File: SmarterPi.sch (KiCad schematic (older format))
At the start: 2 parts, among them J1 Raspberry_Pi_2_3, J2 RJ10

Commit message: Reed
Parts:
- added J3, J4: Screw_Terminal_01x02, TerminalBlock:TerminalBlock_bornier-2_P5.08mm, symbol Connector:Screw_Terminal_01x02
- added R1: 2k4, Resistor_THT:R_Axial_DIN0207_L6.3mm_D2.5mm_P10.16mm_Horizontal, symbol Device:R
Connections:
- net +3V3: now also J3.1 (Pin_1); no longer J1.17 (3V3)
- net GND: now also R1.1
- net REED: now reaches J1.15 (GPIO22)
- net REED: now also J3.2 (Pin_2), R1.2
- no-connect marks 0 -> 3
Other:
- note added: "RJ10 connector for smart meter"
- note added: "Reed connector for gas meter"
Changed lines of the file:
@@
 L power:+3.3V #PWR05
 U 1 1 6019C9EE
-P 5900 2250
-F 0 "#PWR05" H 5900 2100 50  0001 C CNN
-F 1 "+3.3V" H 5915 2423 50  0000 C CNN
-F 2 "" H 5900 2250 50  0001 C CNN
-F 3 "" H 5900 2250 50  0001 C CNN
-	1    5900 2250
+P 5800 2250
+F 0 "#PWR05" H 5800 2100 50  0001 C CNN
+F 1 "+3.3V" H 5815 2423 50  0000 C CNN
+F 2 "" H 5800 2250 50  0001 C CNN
+F 3 "" H 5800 2250 50  0001 C CNN
+	1    5800 2250
 	1    0    0    -1
 $EndComp
 Wire Wire Line
-	5900 2250 5900 2450
-Wire Wire Line
 	5800 2450 5800 2250
-Wire Wire Line
-	5800 2250 5900 2250
-Connection ~ 5900 2250
 $Comp
 L power:PWR_FLAG #FLG01
@@
 Wire Wire Line
 	3350 3000 2950 3000
-Text GLabel 3350 2900 2    50   Input ~ 0
+Wire Wire Line
+	3350 2900 2950 2900
+Wire Wire Line
+	3350 2800 2950 2800
+Text GLabel 4700 2950 0    50   Input ~ 0
+RX
+Wire Wire Line
+	4700 2950 4900 2950
+Text GLabel 4700 2850 0    50   Input ~ 0
 TX
 Wire Wire Line
-	3350 2900 2950 2900
-Text GLabel 3350 2800 2    50   Input ~ 0
+	4700 2850 4900 2850
+Text GLabel 3350 2800 2    50   Output ~ 0
 RX
-Wire Wire Line
-	3350 2800 2950 2800
-Text GLabel 4700 2950 0    50   Output ~ 0
-RX
-Wire Wire Line
-	4700 2950 4900 2950
-Text GLabel 4700 2850 0    50   Output ~ 0
+Text GLabel 3350 2900 2    50   Output ~ 0
 TX
-Wire Wire Line
-	4700 2850 4900 2850
+Wire Notes Line
+	2150 2350 3800 2350
+Wire Notes Line
+	3800 2350 3800 3200
+Wire Notes Line
+	3800 3200 2150 3200
+Wire Notes Line
+	2150 3200 2150 2350
+Text Notes 2150 2350 0    50   ~ 0
+RJ10 connector for smart meter
+$Comp
+L power:+3.3V #PWR08
+U 1 1 601A05BA
+P 3350 4250
+F 0 "#PWR08" H 3350 4100 50  0001 C CNN
+F 1 "+3.3V" V 3365 4378 50  0000 L CNN
+F 2 "" H 3350 4250 50  0001 C CNN
+F 3 "" H 3350 4250 50  0001 C CNN
+	1    3350 4250
+	0    1    1    0
+$EndComp
+Text GLabel 3350 4150 2    50   Output ~ 0
+REED
+Wire Wire Line
+	3350 4250 2750 4250
+Wire Wire Line
+	3350 4150 2850 4150
+Text GLabel 4700 3950 0    50   Input ~ 0
+REED
+Wire Wire Line
+	4700 3950 4900 3950
+$Comp
+L Device:R R1
+U 1 1 601A785D
+P 3150 3950
+F 0 "R1" V 2943 3950 50  0000 C CNN
+F 1 "2k4" V 3034 3950 50  0000 C CNN
+F 2 "Resistor_THT:R_Axial_DIN0207_L6.3mm_D2.5mm_P10.16mm_Horizontal" V 3080 3950 50  0001 C CNN
+F 3 "~" H 3150 3950 50  0001 C CNN
+	1    3150 3950
+	0    1    1    0
+$EndComp
+Wire Wire Line
+	3000 3950 2850 3950
+Wire Wire Line
+	2850 3950 2850 4150
+Connection ~ 2850 4150
+Wire Wire Line
+	2850 4150 2750 4150
+$Comp
+L power:GND #PWR07
+U 1 1 601AC25B
+P 3350 3950
+F 0 "#PWR07" H 3350 3700 50  0001 C CNN
+F 1 "GND" V 3355 3822 50  0000 R CNN
+F 2 "" H 3350 3950 50  0001 C CNN
+F 3 "" H 3350 3950 50  0001 C CNN
+	1    3350 3950
+	0    -1   -1   0
+$EndComp
+Wire Wire Line
+	3350 3950 3300 3950
+Wire Notes Line
+	2150 3650 2150 4400
+Wire Notes Line
+	2150 4400 3800 4400
+Wire Notes Line
+	3800 4400 3800 3650
+Wire Notes Line
+	3800 3650 2150 3650
+Text Notes 2150 3650 0    50   ~ 0
+Reed connector for gas meter
+$Comp
+L Connector:Screw_Terminal_01x02 J3
+U 1 1 6019DF61
+P 2550 4250
+F 0 "J3" H 2468 3925 50  0000 C CNN
+F 1 "Screw_Terminal_01x02" H 2468 4016 50  0000 C CNN
+F 2 "TerminalBlock:TerminalBlock_bornier-2_P5.08mm" H 2550 4250 50  0001 C CNN
+F 3 "~" H 2550 4250 50  0001 C CNN
+	1    2550 4250
+	-1   0    0    1
+$EndComp
+$Comp
+L Connector:Screw_Terminal_01x02 J4
+U 1 1 6019EE56
+P 2550 4800
+F 0 "J4" H 2468 4475 50  0000 C CNN
+F 1 "Screw_Terminal_01x02" H 2468 4566 50  0000 C CNN
+F 2 "TerminalBlock:TerminalBlock_bornier-2_P5.08mm" H 2550 4800 50  0001 C CNN
+F 3 "~" H 2550 4800 50  0001 C CNN
+	1    2550 4800
+	-1   0    0    1
+$EndComp
+NoConn ~ 2750 4700
+NoConn ~ 2750 4800
+NoConn ~ 5900 2450
 $EndSCHEMATC

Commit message: 1Wire
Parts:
- removed J3, J4: Screw_Terminal_01x02, TerminalBlock:TerminalBlock_bornier-2_P5.08mm, symbol Connector:Screw_Terminal_01x02
- added J3: Screw_Terminal_01x04, TerminalBlock_Phoenix:TerminalBlock_Phoenix_MPT-0,5-4-2.54_1x04_P2.54mm_Horizontal, symbol Connector:Screw_Terminal_01x04
- added J4: Screw_Terminal_01x03, TerminalBlock_Phoenix:TerminalBlock_Phoenix_MPT-0,5-3-2.54_1x03_P2.54mm_Horizontal, symbol Connector:Screw_Terminal_01x03
- added R2: 4,7kΩ, Resistor_THT:R_Axial_DIN0207_L6.3mm_D2.5mm_P10.16mm_Horizontal, symbol Device:R
- R1: value 2k4 -> 2,4kΩ
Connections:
- net +3V3: now also J3.1 (Pin_1), J4.1 (Pin_1), R2.2
- net GND: now also J4.3 (Pin_3)
- net REED: now also J3.2 (Pin_2)
- net 1Wire: now reaches J1.7 (GCLK0/GPIO4)
- net 1Wire: now also J4.2 (Pin_2), R2.1
- no-connect marks 3 -> 27
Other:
- note added: "1Wire"
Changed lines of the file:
@@
 P 3150 3950
 F 0 "R1" V 2943 3950 50  0000 C CNN
-F 1 "2k4" V 3034 3950 50  0000 C CNN
+F 1 "2,4kΩ" V 3034 3950 50  0000 C CNN
 F 2 "Resistor_THT:R_Axial_DIN0207_L6.3mm_D2.5mm_P10.16mm_Horizontal" V 3080 3950 50  0001 C CNN
 F 3 "~" H 3150 3950 50  0001 C CNN
@@
 Text Notes 2150 3650 0    50   ~ 0
 Reed connector for gas meter
+NoConn ~ 5900 2450
+NoConn ~ 4900 3150
+NoConn ~ 4900 3250
+NoConn ~ 4900 3350
+NoConn ~ 4900 3550
+NoConn ~ 4900 3650
+NoConn ~ 4900 3750
+NoConn ~ 4900 4050
+NoConn ~ 4900 4150
+NoConn ~ 4900 4250
+NoConn ~ 4900 4350
+NoConn ~ 4900 4450
+NoConn ~ 6500 4550
+NoConn ~ 6500 4450
+NoConn ~ 6500 4250
+NoConn ~ 6500 4150
+NoConn ~ 6500 4050
+NoConn ~ 6500 3950
+NoConn ~ 6500 3850
+NoConn ~ 6500 3650
+NoConn ~ 6500 3550
+NoConn ~ 6500 3250
+NoConn ~ 6500 3150
+NoConn ~ 6500 2950
+NoConn ~ 6500 2850
 $Comp
-L Connector:Screw_Terminal_01x02 J3
-U 1 1 6019DF61
-P 2550 4250
-F 0 "J3" H 2468 3925 50  0000 C CNN
-F 1 "Screw_Terminal_01x02" H 2468 4016 50  0000 C CNN
-F 2 "TerminalBlock:TerminalBlock_bornier-2_P5.08mm" H 2550 4250 50  0001 C CNN
-F 3 "~" H 2550 4250 50  0001 C CNN
-	1    2550 4250
+L Connector:Screw_Terminal_01x04 J3
+U 1 1 601B718F
+P 2550 4150
+F 0 "J3" H 2468 3725 50  0000 C CNN
+F 1 "Screw_Terminal_01x04" H 2468 3816 50  0000 C CNN
+F 2 "TerminalBlock_Phoenix:TerminalBlock_Phoenix_MPT-0,5-4-2.54_1x04_P2.54mm_Horizontal" H 2550 4150 50  0001 C CNN
+F 3 "~" H 2550 4150 50  0001 C CNN
+	1    2550 4150
+	-1   0    0    1
+$EndComp
+NoConn ~ 2750 4050
+NoConn ~ 2750 3950
+$Comp
+L Connector:Screw_Terminal_01x03 J4
+U 1 1 601C3076
+P 2550 5250
+F 0 "J4" H 2468 4925 50  0000 C CNN
+F 1 "Screw_Terminal_01x03" H 2468 5016 50  0000 C CNN
+F 2 "TerminalBlock_Phoenix:TerminalBlock_Phoenix_MPT-0,5-3-2.54_1x03_P2.54mm_Horizontal" H 2550 5250 50  0001 C CNN
+F 3 "~" H 2550 5250 50  0001 C CNN
+	1    2550 5250
 	-1   0    0    1
 $EndComp
 $Comp
-L Connector:Screw_Terminal_01x02 J4
-U 1 1 6019EE56
-P 2550 4800
-F 0 "J4" H 2468 4475 50  0000 C CNN
-F 1 "Screw_Terminal_01x02" H 2468 4566 50  0000 C CNN
-F 2 "TerminalBlock:TerminalBlock_bornier-2_P5.08mm" H 2550 4800 50  0001 C CNN
-F 3 "~" H 2550 4800 50  0001 C CNN
-	1    2550 4800
-	-1   0    0    1
+L power:+3.3V #PWR09
+U 1 1 601CE628
+P 3350 5650
+F 0 "#PWR09" H 3350 5500 50  0001 C CNN
+F 1 "+3.3V" V 3365 5778 50  0000 L CNN
+F 2 "" H 3350 5650 50  0001 C CNN
+F 3 "" H 3350 5650 50  0001 C CNN
+	1    3350 5650
+	0    1    1    0
 $EndComp
-NoConn ~ 2750 4700
-NoConn ~ 2750 4800
-NoConn ~ 5900 2450
+$Comp
+L power:GND #PWR010
+U 1 1 601CFBE1
+P 3350 5150
+F 0 "#PWR010" H 3350 4900 50  0001 C CNN
+F 1 "GND" V 3355 5022 50  0000 R CNN
+F 2 "" H 3350 5150 50  0001 C CNN
+F 3 "" H 3350 5150 50  0001 C CNN
+	1    3350 5150
+	0    -1   -1   0
+$EndComp
+Text GLabel 6750 3450 2    50   Input ~ 0
+1Wire
+Wire Wire Line
+	6500 3450 6750 3450
+Text GLabel 3350 5250 2    50   Output ~ 0
+1Wire
+Wire Wire Line
+	2750 5150 3350 5150
+Wire Wire Line
+	2750 5250 3000 5250
+Wire Wire Line
+	2750 5350 2850 5350
+Wire Wire Line
+	2850 5350 2850 5650
+Wire Wire Line
+	2850 5650 3000 5650
+$Comp
+L Device:R R2
+U 1 1 601E9674
+P 3000 5450
+F 0 "R2" H 3070 5496 50  0000 L CNN
+F 1 "4,7kΩ" H 3070 5405 50  0000 L CNN
+F 2 "Resistor_THT:R_Axial_DIN0207_L6.3mm_D2.5mm_P10.16mm_Horizontal" V 2930 5450 50  0001 C CNN
+F 3 "~" H 3000 5450 50  0001 C CNN
+	1    3000 5450
+	1    0    0    -1
+$EndComp
+Wire Wire Line
+	3000 5300 3000 5250
+Connection ~ 3000 5250
+Wire Wire Line
+	3000 5250 3350 5250
+Wire Wire Line
+	3000 5600 3000 5650
+Connection ~ 3000 5650
+Wire Wire Line
+	3000 5650 3350 5650
+Wire Notes Line
+	2150 4850 3800 4850
+Wire Notes Line
+	3800 4850 3800 5800
+Wire Notes Line
+	3800 5800 2150 5800
+Wire Notes Line
+	2150 5800 2150 4850
+Text Notes 2150 4850 0    50   ~ 0
+1Wire
 $EndSCHEMATC

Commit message: Readme, License, Preview
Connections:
- net +3V3: no longer J4.1 (Pin_1)
- net +5V: now also J4.1 (Pin_1)
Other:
- moved on the sheet: R2
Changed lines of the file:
@@
 	2750 5150 3350 5150
 Wire Wire Line
-	2750 5250 3000 5250
-Wire Wire Line
-	2750 5350 2850 5350
-Wire Wire Line
-	2850 5350 2850 5650
-Wire Wire Line
-	2850 5650 3000 5650
+	2750 5250 3200 5250
 $Comp
 L Device:R R2
 U 1 1 601E9674
-P 3000 5450
-F 0 "R2" H 3070 5496 50  0000 L CNN
-F 1 "4,7kΩ" H 3070 5405 50  0000 L CNN
-F 2 "Resistor_THT:R_Axial_DIN0207_L6.3mm_D2.5mm_P10.16mm_Horizontal" V 2930 5450 50  0001 C CNN
-F 3 "~" H 3000 5450 50  0001 C CNN
-	1    3000 5450
+P 3200 5450
+F 0 "R2" H 3270 5496 50  0000 L CNN
+F 1 "4,7kΩ" H 3270 5405 50  0000 L CNN
+F 2 "Resistor_THT:R_Axial_DIN0207_L6.3mm_D2.5mm_P10.16mm_Horizontal" V 3130 5450 50  0001 C CNN
+F 3 "~" H 3200 5450 50  0001 C CNN
+	1    3200 5450
 	1    0    0    -1
 $EndComp
 Wire Wire Line
-	3000 5300 3000 5250
-Connection ~ 3000 5250
+	3200 5300 3200 5250
+Connection ~ 3200 5250
 Wire Wire Line
-	3000 5250 3350 5250
+	3200 5250 3350 5250
 Wire Wire Line
-	3000 5600 3000 5650
-Connection ~ 3000 5650
+	3200 5600 3200 5650
 Wire Wire Line
-	3000 5650 3350 5650
+	3200 5650 3350 5650
 Wire Notes Line
 	2150 4850 3800 4850
@@
 Text Notes 2150 4850 0    50   ~ 0
 1Wire
+$Comp
+L power:+5V #PWR?
+U 1 1 602F0466
+P 2850 5650
+F 0 "#PWR?" H 2850 5500 50  0001 C CNN
+F 1 "+5V" V 2865 5778 50  0000 L CNN
+F 2 "" H 2850 5650 50  0001 C CNN
+F 3 "" H 2850 5650 50  0001 C CNN
+	1    2850 5650
+	0    1    1    0
+$EndComp
+Wire Wire Line
+	2750 5350 2750 5650
+Wire Wire Line
+	2750 5650 2850 5650
 $EndSCHEMATC

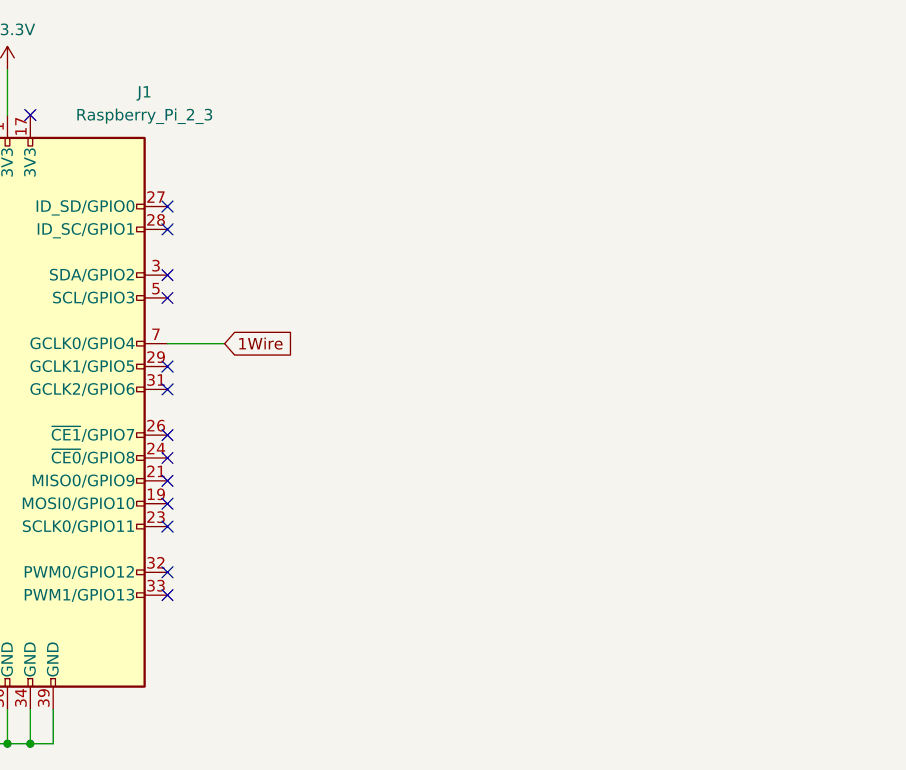
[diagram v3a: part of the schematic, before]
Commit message: Added LEDs
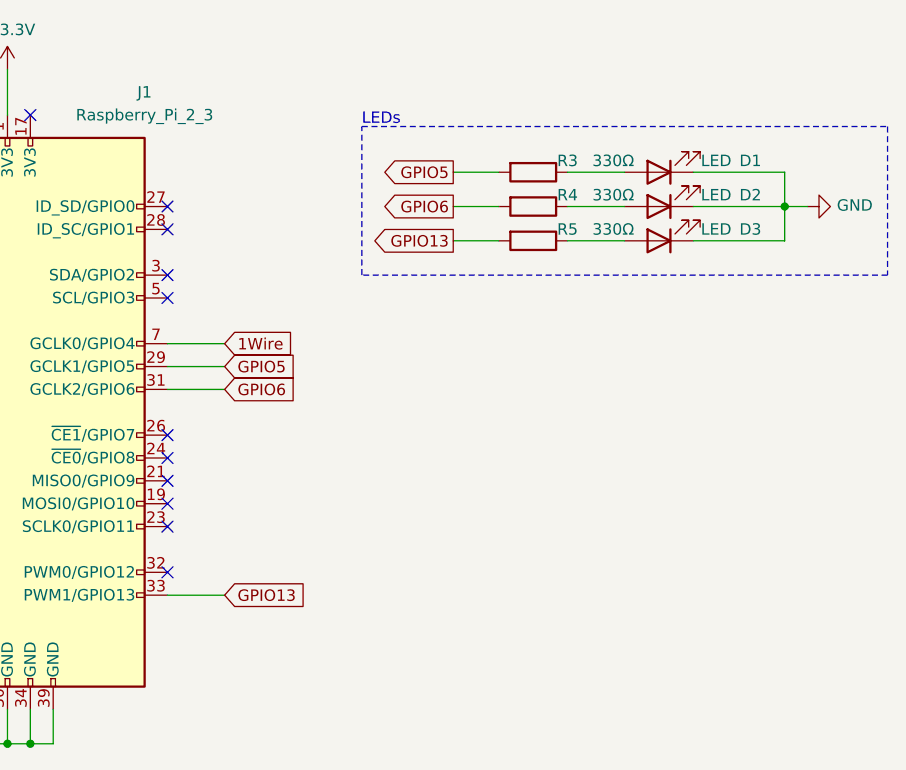
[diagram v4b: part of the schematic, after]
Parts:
- added D1, D2, D3: LED, LED_SMD:LED_0805_2012Metric_Pad1.15x1.40mm_HandSolder, symbol Device:LED
- added R3, R4, R5: 330Ω, Resistor_SMD:R_0805_2012Metric_Pad1.20x1.40mm_HandSolder, symbol Device:R
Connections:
- net GND: now also D1.1 (K), D2.1 (K), D3.1 (K)
- net GPIO5: now reaches J1.29 (GCLK1/GPIO5)
- net GPIO5: now also R3.2
- net GPIO6: now reaches J1.31 (GCLK2/GPIO6)
- net GPIO6: now also R4.2
- net GPIO13: now reaches J1.33 (PWM1/GPIO13)
- net GPIO13: now also R5.2
- new net: D1.2 (A), R3.1
- new net: D2.2 (A), R4.1
- new net: D3.2 (A), R5.1
- no-connect marks 27 -> 24
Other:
- note added: "LEDs"
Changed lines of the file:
@@
 Wire Wire Line
 	4700 3950 4900 3950
-$Comp
-L Device:R R1
-U 1 1 601A785D
-P 3150 3950
-F 0 "R1" V 2943 3950 50  0000 C CNN
-F 1 "2,4kΩ" V 3034 3950 50  0000 C CNN
-F 2 "Resistor_THT:R_Axial_DIN0207_L6.3mm_D2.5mm_P10.16mm_Horizontal" V 3080 3950 50  0001 C CNN
-F 3 "~" H 3150 3950 50  0001 C CNN
-	1    3150 3950
-	0    1    1    0
-$EndComp
 Wire Wire Line
 	3000 3950 2850 3950
@@
 NoConn ~ 4900 4350
 NoConn ~ 4900 4450
-NoConn ~ 6500 4550
 NoConn ~ 6500 4450
 NoConn ~ 6500 4250
@@
 NoConn ~ 6500 3950
 NoConn ~ 6500 3850
-NoConn ~ 6500 3650
-NoConn ~ 6500 3550
 NoConn ~ 6500 3250
 NoConn ~ 6500 3150
@@
 1Wire
 $Comp
-L power:+5V #PWR?
+L power:+5V #PWR011
 U 1 1 602F0466
 P 2850 5650
-F 0 "#PWR?" H 2850 5500 50  0001 C CNN
+F 0 "#PWR011" H 2850 5500 50  0001 C CNN
 F 1 "+5V" V 2865 5778 50  0000 L CNN
 F 2 "" H 2850 5650 50  0001 C CNN
@@
 Wire Wire Line
 	2750 5650 2850 5650
+$Comp
+L Device:LED D1
+U 1 1 602EB0CA
+P 8650 2700
+F 0 "D1" H 8250 2650 50  0000 C CNN
+F 1 "LED" H 8400 2650 50  0000 C CNN
+F 2 "LED_SMD:LED_0805_2012Metric_Pad1.15x1.40mm_HandSolder" H 8650 2700 50  0001 C CNN
+F 3 "~" H 8650 2700 50  0001 C CNN
+	1    8650 2700
+	-1   0    0    1
+$EndComp
+$Comp
+L Device:LED D2
+U 1 1 602EC6AD
+P 8650 2850
+F 0 "D2" H 8250 2800 50  0000 C CNN
+F 1 "LED" H 8400 2800 50  0000 C CNN
+F 2 "LED_SMD:LED_0805_2012Metric_Pad1.15x1.40mm_HandSolder" H 8650 2850 50  0001 C CNN
+F 3 "~" H 8650 2850 50  0001 C CNN
+	1    8650 2850
+	-1   0    0    1
+$EndComp
+$Comp
+L Device:LED D3
+U 1 1 602EEA18
+P 8650 3000
+F 0 "D3" H 8250 2950 50  0000 C CNN
+F 1 "LED" H 8400 2950 50  0000 C CNN
+F 2 "LED_SMD:LED_0805_2012Metric_Pad1.15x1.40mm_HandSolder" H 8650 3000 50  0001 C CNN
+F 3 "~" H 8650 3000 50  0001 C CNN
+	1    8650 3000
+	-1   0    0    1
+$EndComp
+$Comp
+L power:GND #PWR012
+U 1 1 602F08F7
+P 9300 2850
+F 0 "#PWR012" H 9300 2600 50  0001 C CNN
+F 1 "GND" V 9305 2722 50  0000 R CNN
+F 2 "" H 9300 2850 50  0001 C CNN
+F 3 "" H 9300 2850 50  0001 C CNN
+	1    9300 2850
+	0    -1   -1   0
+$EndComp
+Wire Wire Line
+	8800 2700 9200 2700
+Wire Wire Line
+	9200 2700 9200 2850
+Wire Wire Line
+	9200 2850 9300 2850
+Wire Wire Line
+	8800 2850 9200 2850
+Connection ~ 9200 2850
+Wire Wire Line
+	8800 3000 9200 3000
+Wire Wire Line
+	9200 3000 9200 2850
+Wire Wire Line
+	8250 2700 8500 2700
+$Comp
+L Device:R R5
+U 1 1 60300629
+P 8100 3000
+F 0 "R5" V 8050 3150 50  0000 C CNN
+F 1 "330Ω" V 8050 3350 50  0000 C CNN
+F 2 "Resistor_SMD:R_0805_2012Metric_Pad1.20x1.40mm_HandSolder" V 8030 3000 50  0001 C CNN
+F 3 "~" H 8100 3000 50  0001 C CNN
+	1    8100 3000
+	0    1    1    0
+$EndComp
+Wire Wire Line
+	8250 2850 8500 2850
+Wire Wire Line
+	8250 3000 8500 3000
+$Comp
+L Device:R R4
+U 1 1 60300307
+P 8100 2850
+F 0 "R4" V 8050 3000 50  0000 C CNN
+F 1 "330Ω" V 8050 3200 50  0000 C CNN
+F 2 "Resistor_SMD:R_0805_2012Metric_Pad1.20x1.40mm_HandSolder" V 8030 2850 50  0001 C CNN
+F 3 "~" H 8100 2850 50  0001 C CNN
+	1    8100 2850
+	0    1    1    0
+$EndComp
+$Comp
+L Device:R R1
+U 1 1 601A785D
+P 3150 3950
+F 0 "R1" V 2943 3950 50  0000 C CNN
+F 1 "2,4kΩ" V 3034 3950 50  0000 C CNN
+F 2 "Resistor_THT:R_Axial_DIN0207_L6.3mm_D2.5mm_P10.16mm_Horizontal" V 3080 3950 50  0001 C CNN
+F 3 "~" H 3150 3950 50  0001 C CNN
+	1    3150 3950
+	0    1    1    0
+$EndComp
+$Comp
+L Device:R R3
+U 1 1 602FE62D
+P 8100 2700
+F 0 "R3" V 8050 2850 50  0000 C CNN
+F 1 "330Ω" V 8050 3050 50  0000 C CNN
+F 2 "Resistor_SMD:R_0805_2012Metric_Pad1.20x1.40mm_HandSolder" V 8030 2700 50  0001 C CNN
+F 3 "~" H 8100 2700 50  0001 C CNN
+	1    8100 2700
+	0    1    1    0
+$EndComp
+Text GLabel 6750 3550 2    50   Input ~ 0
+GPIO5
+Text GLabel 6750 3650 2    50   Input ~ 0
+GPIO6
+Text GLabel 6750 4550 2    50   Input ~ 0
+GPIO13
+Wire Wire Line
+	6500 4550 6750 4550
+Wire Wire Line
+	6500 3550 6750 3550
+Wire Wire Line
+	6500 3650 6750 3650
+Text GLabel 7750 2700 0    50   Output ~ 0
+GPIO5
+Wire Wire Line
+	7750 2700 7950 2700
+Text GLabel 7750 2850 0    50   Output ~ 0
+GPIO6
+Wire Wire Line
+	7750 2850 7950 2850
+Text GLabel 7750 3000 0    50   Output ~ 0
+GPIO13
+Wire Wire Line
+	7750 3000 7950 3000
+Wire Notes Line
+	7350 2500 9650 2500
+Wire Notes Line
+	9650 2500 9650 3150
+Wire Notes Line
+	9650 3150 7350 3150
+Wire Notes Line
+	7350 3150 7350 2500
+Text Notes 7350 2500 0    50   ~ 0
+LEDs
 $EndSCHEMATC
